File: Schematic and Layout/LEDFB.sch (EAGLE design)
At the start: 25 parts, among them U1 TLV61225L

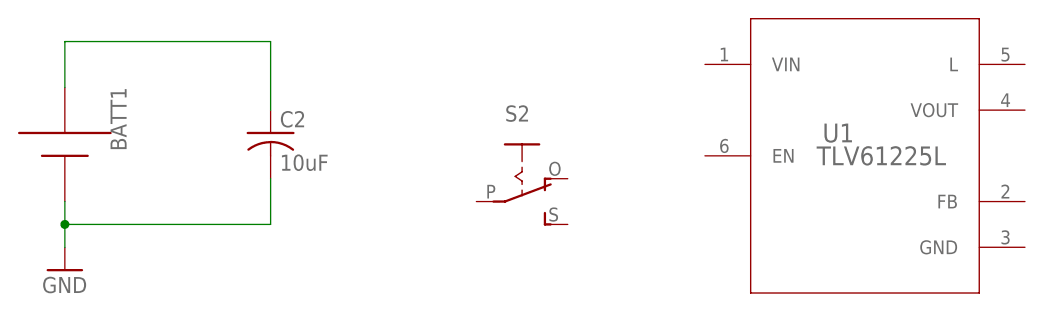
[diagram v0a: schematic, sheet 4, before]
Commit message: Added itg3701 library, added a gitignore document to ignore autosave files, added reference docs
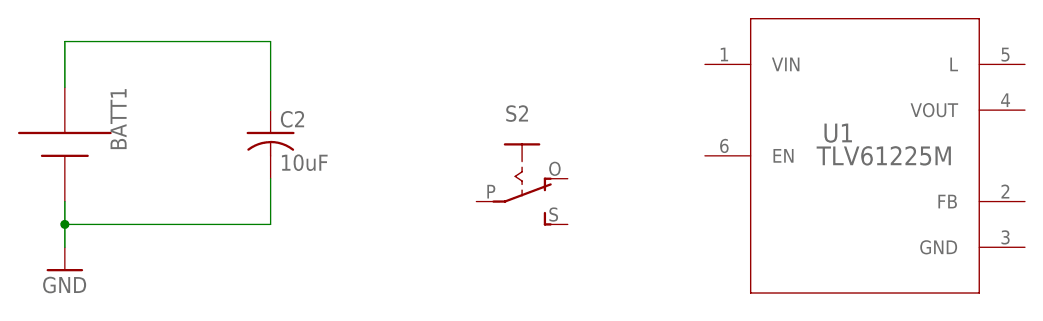
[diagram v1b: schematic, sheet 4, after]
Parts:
- added U2: ITG-37013X3MM, itg_3701:ITG-37013X3MM
- U1: value TLV61225L -> TLV61225M; device TLV61225:TLV61225L -> TLV61225:TLV61225M
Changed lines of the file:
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@@
 <grid distance="0.1" unitdist="inch" unit="inch" style="lines" multiple="1" display="no" altdistance="0.01" altunitdist="inch" altunit="inch"/>
 <layers>
-<layer number="1" name="Top" color="4" fill="1" visible="no" active="no"/>
-<layer number="2" name="Route2" color="1" fill="3" visible="no" active="no"/>
-<layer number="3" name="Route3" color="4" fill="3" visible="no" active="no"/>
-<layer number="4" name="Route4" color="1" fill="4" visible="no" active="no"/>
-<layer number="5" name="Route5" color="4" fill="4" visible="no" active="no"/>
-<layer number="6" name="Route6" color="1" fill="8" visible="no" active="no"/>
-<layer number="7" name="Route7" color="4" fill="8" visible="no" active="no"/>
-<layer number="8" name="Route8" color="1" fill="2" visible="no" active="no"/>
-<layer number="9" name="Route9" color="4" fill="2" visible="no" active="no"/>
-<layer number="10" name="Route10" color="1" fill="7" visible="no" active="no"/>
-<layer number="11" name="Route11" color="4" fill="7" visible="no" active="no"/>
-<layer number="12" name="Route12" color="1" fill="5" visible="no" active="no"/>
-<layer number="13" name="Route13" color="4" fill="5" visible="no" active="no"/>
-<layer number="14" name="Route14" color="1" fill="6" visible="no" active="no"/>
-<layer number="15" name="Route15" color="4" fill="6" visible="no" active="no"/>
-<layer number="16" name="Bottom" color="1" fill="1" visible="no" active="no"/>
-<layer number="17" name="Pads" color="2" fill="1" visible="no" active="no"/>
-<layer number="18" name="Vias" color="2" fill="1" visible="no" active="no"/>
-<layer number="19" name="Unrouted" color="6" fill="1" visible="no" active="no"/>
-<layer number="20" name="Dimension" color="15" fill="1" visible="no" active="no"/>
-<layer number="21" name="tPlace" color="7" fill="1" visible="no" active="no"/>
-<layer number="22" name="bPlace" color="7" fill="1" visible="no" active="no"/>
-<layer number="23" name="tOrigins" color="15" fill="1" visible="no" active="no"/>
-<layer number="24" name="bOrigins" color="15" fill="1" visible="no" active="no"/>
-<layer number="25" name="tNames" color="7" fill="1" visible="no" active="no"/>
-<layer number="26" name="bNames" color="7" fill="1" visible="no" active="no"/>
-<layer number="27" name="tValues" color="7" fill="1" visible="no" active="no"/>
-<layer number="28" name="bValues" color="7" fill="1" visible="no" active="no"/>
+<layer number="1" name="Top" color="4" fill="1" visible="yes" active="no"/>
+<layer number="2" name="Route2" color="1" fill="3" visible="yes" active="no"/>
+<layer number="3" name="Route3" color="4" fill="3" visible="yes" active="no"/>
+<layer number="4" name="Route4" color="1" fill="4" visible="yes" active="no"/>
+<layer number="5" name="Route5" color="4" fill="4" visible="yes" active="no"/>
+<layer number="6" name="Route6" color="1" fill="8" visible="yes" active="no"/>
+<layer number="7" name="Route7" color="4" fill="8" visible="yes" active="no"/>
+<layer number="8" name="Route8" color="1" fill="2" visible="yes" active="no"/>
+<layer number="9" name="Route9" color="4" fill="2" visible="yes" active="no"/>
+<layer number="10" name="Route10" color="1" fill="7" visible="yes" active="no"/>
+<layer number="11" name="Route11" color="4" fill="7" visible="yes" active="no"/>
+<layer number="12" name="Route12" color="1" fill="5" visible="yes" active="no"/>
+<layer number="13" name="Route13" color="4" fill="5" visible="yes" active="no"/>
+<layer number="14" name="Route14" color="1" fill="6" visible="yes" active="no"/>
+<layer number="15" name="Route15" color="4" fill="6" visible="yes" active="no"/>
+<layer number="16" name="Bottom" color="1" fill="1" visible="yes" active="no"/>
+<layer number="17" name="Pads" color="2" fill="1" visible="yes" active="no"/>
+<layer number="18" name="Vias" color="2" fill="1" visible="yes" active="no"/>
+<layer number="19" name="Unrouted" color="6" fill="1" visible="yes" active="no"/>
+<layer number="20" name="Dimension" color="15" fill="1" visible="yes" active="no"/>
+<layer number="21" name="tPlace" color="7" fill="1" visible="yes" active="no"/>
+<layer number="22" name="bPlace" color="7" fill="1" visible="yes" active="no"/>
+<layer number="23" name="tOrigins" color="15" fill="1" visible="yes" active="no"/>
+<layer number="24" name="bOrigins" color="15" fill="1" visible="yes" active="no"/>
+<layer number="25" name="tNames" color="7" fill="1" visible="yes" active="no"/>
+<layer number="26" name="bNames" color="7" fill="1" visible="yes" active="no"/>
+<layer number="27" name="tValues" color="7" fill="1" visible="yes" active="no"/>
+<layer number="28" name="bValues" color="7" fill="1" visible="yes" active="no"/>
 <layer number="29" name="tStop" color="7" fill="3" visible="no" active="no"/>
 <layer number="30" name="bStop" color="7" fill="6" visible="no" active="no"/>
@@
 <layer number="35" name="tGlue" color="7" fill="4" visible="no" active="no"/>
 <layer number="36" name="bGlue" color="7" fill="5" visible="no" active="no"/>
-<layer number="37" name="tTest" color="7" fill="1" visible="no" active="no"/>
-<layer number="38" name="bTest" color="7" fill="1" visible="no" active="no"/>
+<layer number="37" name="tTest" color="7" fill="1" visible="yes" active="no"/>
+<layer number="38" name="bTest" color="7" fill="1" visible="yes" active="no"/>
 <layer number="39" name="tKeepout" color="4" fill="11" visible="no" active="no"/>
 <layer number="40" name="bKeepout" color="1" fill="11" visible="no" active="no"/>
@@
 <layer number="44" name="Drills" color="7" fill="1" visible="no" active="no"/>
 <layer number="45" name="Holes" color="7" fill="1" visible="no" active="no"/>
-<layer number="46" name="Milling" color="3" fill="1" visible="no" active="no"/>
-<layer number="47" name="Measures" color="7" fill="1" visible="no" active="no"/>
-<layer number="48" name="Document" color="7" fill="1" visible="no" active="no"/>
-<layer number="49" name="Reference" color="7" fill="1" visible="no" active="no"/>
-<layer number="50" name="dxf" color="7" fill="1" visible="no" active="no"/>
-<layer number="51" name="tDocu" color="7" fill="1" visible="no" active="no"/>
-<layer number="52" name="bDocu" color="7" fill="1" visible="no" active="no"/>
-<layer number="53" name="tGND_GNDA" color="7" fill="9" visible="no" active="no"/>
-<layer number="54" name="bGND_GNDA" color="1" fill="9" visible="no" active="no"/>
-<layer number="56" name="wert" color="7" fill="1" visible="no" active="no"/>
-<layer number="57" name="tCAD" color="7" fill="1" visible="no" active="no"/>
-<layer number="59" name="tCarbon" color="7" fill="1" visible="no" active="no"/>
-<layer number="60" name="bCarbon" color="7" fill="1" visible="no" active="no"/>
+<layer number="46" name="Milling" color="3" fill="1" visible="yes" active="no"/>
+<layer number="47" name="Measures" color="7" fill="1" visible="yes" active="no"/>
+<layer number="48" name="Document" color="7" fill="1" visible="yes" active="no"/>
+<layer number="49" name="Reference" color="7" fill="1" visible="yes" active="no"/>
+<layer number="50" name="dxf" color="7" fill="1" visible="yes" active="no"/>
+<layer number="51" name="tDocu" color="7" fill="1" visible="yes" active="no"/>
+<layer number="52" name="bDocu" color="7" fill="1" visible="yes" active="no"/>
+<layer number="53" name="tGND_GNDA" color="7" fill="9" visible="yes" active="no"/>
+<layer number="54" name="bGND_GNDA" color="1" fill="9" visible="yes" active="no"/>
+<layer number="56" name="wert" color="7" fill="1" visible="yes" active="no"/>
+<layer number="57" name="tCAD" color="7" fill="1" visible="yes" active="no"/>
+<layer number="59" name="tCarbon" color="7" fill="1" visible="yes" active="no"/>
+<layer number="60" name="bCarbon" color="7" fill="1" visible="yes" active="no"/>
 <layer number="90" name="Modules" color="7" fill="1" visible="no" active="yes"/>
 <layer number="91" name="Nets" color="2" fill="1" visible="yes" active="yes"/>
@@
 <part name="C2" library="adafruit" deviceset="C-US" device="C0805" value="10uF"/>
 <part name="S2" library="adafruit" deviceset="EG1218" device="S"/>
-<part name="U1" library="TLV61225" deviceset="TLV61225" device="L"/>
+<part name="U1" library="TLV61225" deviceset="TLV61225" device="M" value="TLV61225M"/>
+<part name="U2" library="itg_3701" deviceset="ITG-3701" device="3X3MM"/>
 </parts>
 <sheets>
@@
 </plain>
 <instances>
+<instance part="U2" gate="A" x="0" y="2.54"/>
 </instances>
 <busses>
